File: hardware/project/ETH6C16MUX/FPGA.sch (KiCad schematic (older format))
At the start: 6 parts

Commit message: Schematic design
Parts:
- U? (x6): symbol ETH6C12MUX:iCE40HX4K-TQ144 -> ETH6C16MUX:iCE40HX4K-TQ144
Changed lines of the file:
@@
 EESchema Schematic File Version 4
-LIBS:ETH6C12MUX-cache
+LIBS:ETH6C16MUX-cache
 EELAYER 30 0
 EELAYER END
 $Descr A4 11693 8268
 encoding utf-8
-Sheet 5 8
+Sheet 4 8
 Title ""
 Date ""
@@
 $EndDescr
 $Comp
-L ETH6C12MUX:iCE40HX4K-TQ144 U?
+L ETH6C16MUX:iCE40HX4K-TQ144 U?
 U 1 1 5D7691C2
 P 2500 2550
@@
 $EndComp
 $Comp
-L ETH6C12MUX:iCE40HX4K-TQ144 U?
+L ETH6C16MUX:iCE40HX4K-TQ144 U?
 U 2 1 5D76B1F4
 P 4850 2600
@@
 $EndComp
 $Comp
-L ETH6C12MUX:iCE40HX4K-TQ144 U?
+L ETH6C16MUX:iCE40HX4K-TQ144 U?
 U 3 1 5D76D216
 P 7150 2600
@@
 $EndComp
 $Comp
-L ETH6C12MUX:iCE40HX4K-TQ144 U?
+L ETH6C16MUX:iCE40HX4K-TQ144 U?
 U 4 1 5D770CE5
 P 9350 2600
@@
 $EndComp
 $Comp
-L ETH6C12MUX:iCE40HX4K-TQ144 U?
+L ETH6C16MUX:iCE40HX4K-TQ144 U?
 U 5 1 5D7741C3
 P 5550 4750
@@
 $EndComp
 $Comp
-L ETH6C12MUX:iCE40HX4K-TQ144 U?
+L ETH6C16MUX:iCE40HX4K-TQ144 U?
 U 6 1 5D77956C
 P 2500 5100

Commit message: FPGA schematic
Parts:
- removed U? (x6): iCE40HX4K-TQ144, symbol ETH6C16MUX:iCE40HX4K-TQ144
- added C? (x2): 100n, symbol Device:C
- added C?: 47n, symbol Device:C
- added C? (x4): 1u, symbol Device:C
- added R?: 0, symbol Device:R
- added U? (x6): iCE40-HX4K-TQ144, symbol ETH6C16MUX:iCE40-HX4K-TQ144
- added U?: ASDM1-20.000MHZ-LC-T, Oscillator:Oscillator_SMD_Abracon_ASDMB-4Pin_2.5x2.0mm, symbol Oscillator:ASDMB-xxxMHz
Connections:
- net labels added: +1.2V_FPGA_VCC, +1.2V_PLL_VCC, +2.5V_FPGA_VCC, +3.3V_FPGA, CTRI_10A, CTRI_10B, CTRI_10C, CTRI_11A, CTRI_11B, CTRI_11C, CTRI_12A, CTRI_12B, CTRI_12C, CTRI_13A, CTRI_13B, CTRI_13C, CTRI_14A, CTRI_14B, CTRI_14C, CTRI_15A, CTRI_15B, CTRI_15C, CTRI_16A, CTRI_16B, CTRI_16C, CTRI_1A, CTRI_1B, CTRI_1C, CTRI_2A, CTRI_2B, CTRI_2C, CTRI_3A, CTRI_3B, CTRI_3C, CTRI_4A, CTRI_4B, CTRI_4C, CTRI_5A, CTRI_5B, CTRI_5C, CTRI_6A, CTRI_6B, CTRI_6C, CTRI_7A, CTRI_7B, CTRI_7C, CTRI_8A, CTRI_8B, CTRI_8C, CTRI_9A, CTRI_9B, CTRI_9C, CTRI_A, CTRI_B, CTRI_C, CTRI_D, CTRI_E, CTRI_F, FPGA_20MHZ_REF, FPGA_CBSEL0, FPGA_CBSEL1, FPGA_CDONE, FPGA_CFG_CS, FPGA_CRESET_B, FPGA_SPI3_CS, GND, MCU_SPI3_MISO, MCU_SPI3_MOSI, MCU_SPI3_SCLK, RELAY_CTR
- wire segments 0 -> 113
- no-connect marks 0 -> 1

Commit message: Schematic design
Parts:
- removed C?: 47n, symbol Device:C
- added C401, C403: 10u, symbol Device:C
- added C402, C404: 100n, ETH6C16MXU:C_0603_A_Pad1.05x0.95mm_HandSolder, symbol Device:C
- added D401: CDBU0520, symbol Device:D_Schottky
- added R401, R404: 100, symbol Device:R
- added R402: 220, symbol Device:R
- C405, C410: renamed from C?; footprint (none) -> ETH6C16MXU:C_0603_A_Pad1.05x0.95mm_HandSolder
- U401: renamed from U?; footprint (none) -> Package_QFP:TQFP-144_20x20mm_P0.5mm
- U402: renamed from U?; value ASDM1-20.000MHZ-LC-T -> ASDM1-100.000MHZ-LC-T
- gave numbers to parts that had none: 5
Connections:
- net labels added: +3.3V, FPGA1_CBSEL0, FPGA1_CBSEL1, FPGA1_CDONE, FPGA1_CFG_CS, FPGA1_CRESET_B, FPGA1_SPI5_CS, FPGA1_SPI5_MISO, FPGA1_SPI5_MOSI, FPGA1_SPI5_SLCK, FPGA_100MHZ_REF, RELAY0, RELAY1, RELAY10, RELAY11, RELAY12, RELAY13, RELAY14, RELAY15, RELAY16, RELAY17, RELAY18, RELAY19, RELAY2, RELAY20, RELAY21, RELAY22, RELAY23, RELAY24, RELAY25, RELAY26, RELAY27, RELAY28, RELAY29, RELAY3, RELAY30, RELAY31, RELAY32, RELAY33, RELAY34, RELAY35, RELAY36, RELAY37, RELAY38, RELAY39, RELAY4, RELAY40, RELAY41, RELAY42, RELAY43, RELAY44, RELAY45, RELAY46, RELAY47, RELAY48, RELAY49, RELAY5, RELAY50, RELAY51, RELAY52, RELAY53, RELAY6, RELAY7, RELAY8, RELAY9, RELAY[0..53]
- net labels removed: +1.2V_PLL_VCC, +2.5V_FPGA_VCC, +3.3V_FPGA, CTRI_10A, CTRI_10B, CTRI_10C, CTRI_11A, CTRI_11B, CTRI_11C, CTRI_12A, CTRI_12B, CTRI_12C, CTRI_13A, CTRI_13B, CTRI_13C, CTRI_14A, CTRI_14B, CTRI_14C, CTRI_15A, CTRI_15B, CTRI_15C, CTRI_16A, CTRI_16B, CTRI_16C, CTRI_1A, CTRI_1B, CTRI_1C, CTRI_2A, CTRI_2B, CTRI_2C, CTRI_3A, CTRI_3B, CTRI_3C, CTRI_4A, CTRI_4B, CTRI_4C, CTRI_5A, CTRI_5B, CTRI_5C, CTRI_6A, CTRI_6B, CTRI_6C, CTRI_7A, CTRI_7B, CTRI_7C, CTRI_8A, CTRI_8B, CTRI_8C, CTRI_9A, CTRI_9B, CTRI_9C, CTRI_A, CTRI_B, CTRI_C, CTRI_D, CTRI_E, CTRI_F, FPGA_20MHZ_REF, FPGA_CBSEL0, FPGA_CBSEL1, FPGA_CDONE, FPGA_CFG_CS, FPGA_CRESET_B, FPGA_SPI3_CS, RELAY_CTR
- wire segments 113 -> 134
- no-connect marks 1 -> 43
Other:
- moved on the sheet: C405, C406, C407, C408, C409, C410, R403, U401A, U401B, U401C, U401D, U401E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

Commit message: PCB design, need to redesign of the board to board connectors.
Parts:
- C401, C403: footprint (none) -> Capacitor_SMD:C_0805_2012Metric_Pad1.15x1.40mm_HandSolder
- C406, C407, C408, C409: footprint (none) -> ETH6C16MXU:C_0603_B_Pad1.05x0.95mm_HandSolder
- D401: footprint (none) -> Diode_SMD:D_SOD-523
- R401, R402, R403, R404: footprint (none) -> Resistor_SMD:R_0603_1608Metric_Pad1.05x0.95mm_HandSolder
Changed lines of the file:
@@
 F 0 "R403" V 9450 5200 50  0000 C CNN
 F 1 "0" V 9550 5200 50  0000 C CNN
-F 2 "" V 9580 5200 50  0001 C CNN
+F 2 "Resistor_SMD:R_0603_1608Metric_Pad1.05x0.95mm_HandSolder" V 9580 5200 50  0001 C CNN
 F 3 "~" H 9650 5200 50  0001 C CNN
 	1    9650 5200
@@
 F 0 "C406" H 815 7296 50  0000 L CNN
 F 1 "1u" H 815 7205 50  0000 L CNN
-F 2 "" H 738 7100 50  0001 C CNN
+F 2 "ETH6C16MXU:C_0603_B_Pad1.05x0.95mm_HandSolder" H 738 7100 50  0001 C CNN
 F 3 "~" H 700 7250 50  0001 C CNN
 	1    700  7250
@@
 F 0 "C407" H 1315 7296 50  0000 L CNN
 F 1 "1u" H 1315 7205 50  0000 L CNN
-F 2 "" H 1238 7100 50  0001 C CNN
+F 2 "ETH6C16MXU:C_0603_B_Pad1.05x0.95mm_HandSolder" H 1238 7100 50  0001 C CNN
 F 3 "~" H 1200 7250 50  0001 C CNN
 	1    1200 7250
@@
 F 0 "C408" H 1815 7296 50  0000 L CNN
 F 1 "1u" H 1815 7205 50  0000 L CNN
-F 2 "" H 1738 7100 50  0001 C CNN
+F 2 "ETH6C16MXU:C_0603_B_Pad1.05x0.95mm_HandSolder" H 1738 7100 50  0001 C CNN
 F 3 "~" H 1700 7250 50  0001 C CNN
 	1    1700 7250
@@
 F 0 "C409" H 2315 7296 50  0000 L CNN
 F 1 "1u" H 2315 7205 50  0000 L CNN
-F 2 "" H 2238 7100 50  0001 C CNN
+F 2 "ETH6C16MXU:C_0603_B_Pad1.05x0.95mm_HandSolder" H 2238 7100 50  0001 C CNN
 F 3 "~" H 2200 7250 50  0001 C CNN
 	1    2200 7250
@@
 F 0 "R402" V 2093 4950 50  0000 C CNN
 F 1 "220" V 2184 4950 50  0000 C CNN
-F 2 "" V 2230 4950 50  0001 C CNN
+F 2 "Resistor_SMD:R_0603_1608Metric_Pad1.05x0.95mm_HandSolder" V 2230 4950 50  0001 C CNN
 F 3 "~" H 2300 4950 50  0001 C CNN
 	1    2300 4950
@@
 F 0 "C401" H 5365 4746 50  0000 L CNN
 F 1 "10u" H 5365 4655 50  0000 L CNN
-F 2 "" H 5288 4550 50  0001 C CNN
+F 2 "Capacitor_SMD:C_0805_2012Metric_Pad1.15x1.40mm_HandSolder" H 5288 4550 50  0001 C CNN
 F 3 "~" H 5250 4700 50  0001 C CNN
 	1    5250 4700
@@
 F 0 "R401" V 4793 4900 50  0000 C CNN
 F 1 "100" V 4884 4900 50  0000 C CNN
-F 2 "" V 4930 4900 50  0001 C CNN
+F 2 "Resistor_SMD:R_0603_1608Metric_Pad1.05x0.95mm_HandSolder" V 4930 4900 50  0001 C CNN
 F 3 "~" H 5000 4900 50  0001 C CNN
 	1    5000 4900
@@
 F 0 "C403" H 5365 5246 50  0000 L CNN
 F 1 "10u" H 5365 5155 50  0000 L CNN
-F 2 "" H 5288 5050 50  0001 C CNN
+F 2 "Capacitor_SMD:C_0805_2012Metric_Pad1.15x1.40mm_HandSolder" H 5288 5050 50  0001 C CNN
 F 3 "~" H 5250 5200 50  0001 C CNN
 	1    5250 5200
@@
 F 0 "R404" V 4793 5400 50  0000 C CNN
 F 1 "100" V 4884 5400 50  0000 C CNN
-F 2 "" V 4930 5400 50  0001 C CNN
+F 2 "Resistor_SMD:R_0603_1608Metric_Pad1.05x0.95mm_HandSolder" V 4930 5400 50  0001 C CNN
 F 3 "~" H 5000 5400 50  0001 C CNN
 	1    5000 5400
@@
 F 0 "D401" H 6200 5684 50  0000 C CNN
 F 1 "CDBU0520" H 6200 5775 50  0000 C CNN
-F 2 "" H 6200 5900 50  0001 C CNN
+F 2 "Diode_SMD:D_SOD-523" H 6200 5900 50  0001 C CNN
 F 3 "~" H 6200 5900 50  0001 C CNN
 	1    6200 5900

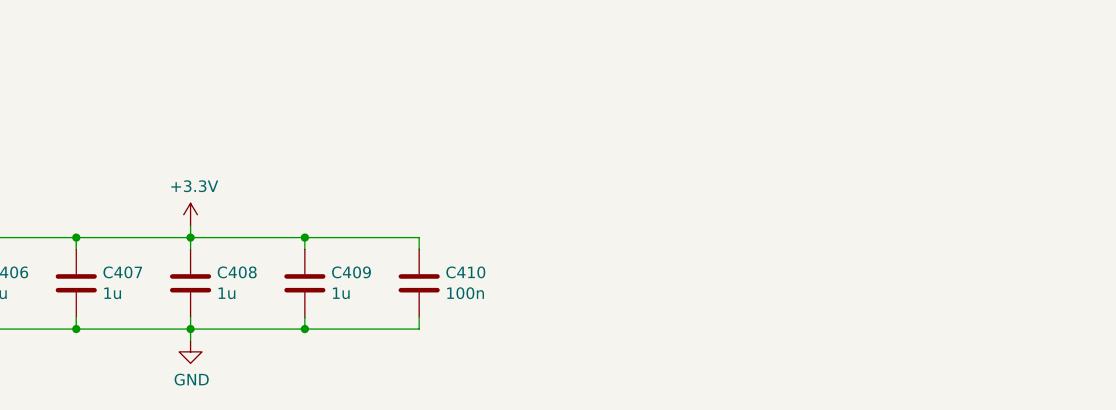
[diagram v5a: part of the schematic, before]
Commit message: PCB layout, deleted USB.
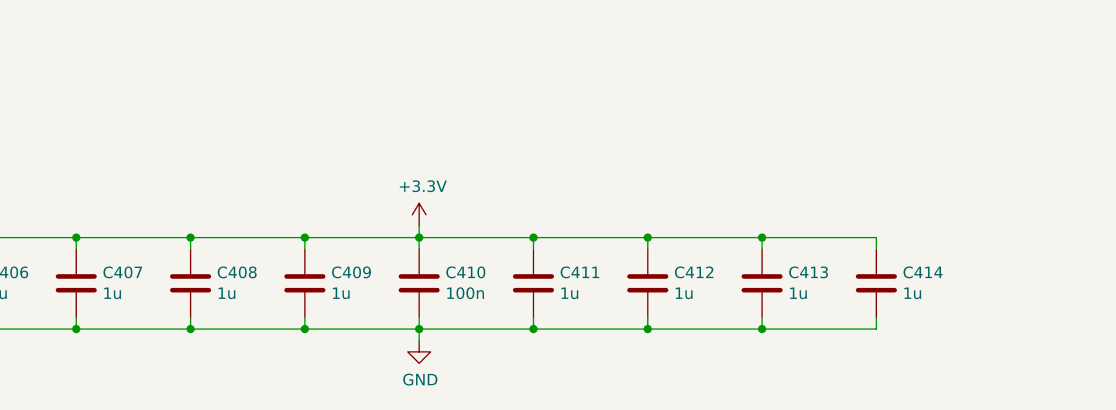
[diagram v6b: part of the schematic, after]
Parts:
- added C411, C412, C413, C414: 1u, ETH6C16MXU:C_0603_B_Pad1.05x0.95mm_HandSolder, symbol Device:C
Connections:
- net +3V3: now also C411.1, C412.1, C413.1, C414.1
- net GND: now also C411.2, C412.2, C413.2, C414.2
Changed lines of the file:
@@
 $Descr A4 11693 8268
 encoding utf-8
-Sheet 4 8
+Sheet 4 7
 Title ""
 Date ""
@@
 $EndComp
 $Comp
-L power:GND #PWR0414
-U 1 1 5DDE0555
-P 1700 7500
-F 0 "#PWR0414" H 1700 7250 50  0001 C CNN
-F 1 "GND" H 1705 7327 50  0000 C CNN
-F 2 "" H 1700 7500 50  0001 C CNN
-F 3 "" H 1700 7500 50  0001 C CNN
-	1    1700 7500
-	1    0    0    -1
-$EndComp
-$Comp
 L Device:C C407
 U 1 1 5DDE07CE
@@
 Connection ~ 1200 7050
 Wire Wire Line
-	1700 7500 1700 7450
-Wire Wire Line
-	1700 7000 1700 7050
+	2700 7000 2700 7050
 $Comp
 L Device:C C410
@@
 L power:+3.3V #PWR0413
 U 1 1 5DAA6483
-P 1700 7000
-F 0 "#PWR0413" H 1700 6850 50  0001 C CNN
-F 1 "+3.3V" H 1715 7173 50  0000 C CNN
-F 2 "" H 1700 7000 50  0001 C CNN
-F 3 "" H 1700 7000 50  0001 C CNN
-	1    1700 7000
+P 2700 7000
+F 0 "#PWR0413" H 2700 6850 50  0001 C CNN
+F 1 "+3.3V" H 2715 7173 50  0000 C CNN
+F 2 "" H 2700 7000 50  0001 C CNN
+F 3 "" H 2700 7000 50  0001 C CNN
+	1    2700 7000
 	1    0    0    -1
 $EndComp
@@
 Wire Wire Line
 	2000 2300 1950 2300
+$Comp
+L Device:C C411
+U 1 1 5D90990C
+P 3200 7250
+F 0 "C411" H 3315 7296 50  0000 L CNN
+F 1 "1u" H 3315 7205 50  0000 L CNN
+F 2 "ETH6C16MXU:C_0603_B_Pad1.05x0.95mm_HandSolder" H 3238 7100 50  0001 C CNN
+F 3 "~" H 3200 7250 50  0001 C CNN
+	1    3200 7250
+	1    0    0    -1
+$EndComp
+$Comp
+L Device:C C412
+U 1 1 5D909912
+P 3700 7250
+F 0 "C412" H 3815 7296 50  0000 L CNN
+F 1 "1u" H 3815 7205 50  0000 L CNN
+F 2 "ETH6C16MXU:C_0603_B_Pad1.05x0.95mm_HandSolder" H 3738 7100 50  0001 C CNN
+F 3 "~" H 3700 7250 50  0001 C CNN
+	1    3700 7250
+	1    0    0    -1
+$EndComp
+$Comp
+L Device:C C413
+U 1 1 5D909918
+P 4200 7250
+F 0 "C413" H 4315 7296 50  0000 L CNN
+F 1 "1u" H 4315 7205 50  0000 L CNN
+F 2 "ETH6C16MXU:C_0603_B_Pad1.05x0.95mm_HandSolder" H 4238 7100 50  0001 C CNN
+F 3 "~" H 4200 7250 50  0001 C CNN
+	1    4200 7250
+	1    0    0    -1
+$EndComp
+$Comp
+L Device:C C414
+U 1 1 5D90991E
+P 4700 7250
+F 0 "C414" H 4815 7296 50  0000 L CNN
+F 1 "1u" H 4815 7205 50  0000 L CNN
+F 2 "ETH6C16MXU:C_0603_B_Pad1.05x0.95mm_HandSolder" H 4738 7100 50  0001 C CNN
+F 3 "~" H 4700 7250 50  0001 C CNN
+	1    4700 7250
+	1    0    0    -1
+$EndComp
+Wire Wire Line
+	4700 7450 4700 7400
+Connection ~ 2700 7450
+Wire Wire Line
+	4700 7100 4700 7050
+Wire Wire Line
+	4700 7050 4200 7050
+Connection ~ 2700 7050
+Wire Wire Line
+	3200 7100 3200 7050
+Connection ~ 3200 7050
+Wire Wire Line
+	3200 7050 2700 7050
+Wire Wire Line
+	3200 7400 3200 7450
+Connection ~ 3200 7450
+Wire Wire Line
+	3200 7450 3700 7450
+Wire Wire Line
+	3700 7400 3700 7450
+Connection ~ 3700 7450
+Wire Wire Line
+	3700 7450 4200 7450
+Wire Wire Line
+	3700 7100 3700 7050
+Connection ~ 3700 7050
+Wire Wire Line
+	3700 7050 3200 7050
+Wire Wire Line
+	4200 7100 4200 7050
+Connection ~ 4200 7050
+Wire Wire Line
+	4200 7050 3700 7050
+Wire Wire Line
+	4200 7400 4200 7450
+Connection ~ 4200 7450
+Wire Wire Line
+	4200 7450 4700 7450
+Wire Wire Line
+	2700 7450 3200 7450
+Wire Wire Line
+	2700 7500 2700 7450
+$Comp
+L power:GND #PWR0414
+U 1 1 5DDE0555
+P 2700 7500
+F 0 "#PWR0414" H 2700 7250 50  0001 C CNN
+F 1 "GND" H 2705 7327 50  0000 C CNN
+F 2 "" H 2700 7500 50  0001 C CNN
+F 3 "" H 2700 7500 50  0001 C CNN
+	1    2700 7500
+	1    0    0    -1
+$EndComp
 Wire Bus Line
 	3650 750  3650 3650

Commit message: Deleted FPGA part and change it for SPI IO chips. Change power supply circuit.
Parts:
- C402, C404, C405, C410: footprint ETH6C16MXU:C_0603_A_Pad1.05x0.95mm_HandSolder -> Capacitor_SMD:C_0603_1608Metric_Pad1.05x0.95mm_HandSolder
- C406, C407, C408, C409, C411, C412, C413, C414: footprint ETH6C16MXU:C_0603_B_Pad1.05x0.95mm_HandSolder -> Capacitor_SMD:C_0603_1608Metric_Pad1.05x0.95mm_HandSolder
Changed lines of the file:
@@
 F 0 "C405" H 1035 5346 50  0000 R CNN
 F 1 "100n" H 1035 5255 50  0000 R CNN
-F 2 "ETH6C16MXU:C_0603_A_Pad1.05x0.95mm_HandSolder" H 1188 5150 50  0001 C CNN
+F 2 "Capacitor_SMD:C_0603_1608Metric_Pad1.05x0.95mm_HandSolder" H 1188 5150 50  0001 C CNN
 F 3 "~" H 1150 5300 50  0001 C CNN
 	1    1150 5300
@@
 F 0 "C406" H 815 7296 50  0000 L CNN
 F 1 "1u" H 815 7205 50  0000 L CNN
-F 2 "ETH6C16MXU:C_0603_B_Pad1.05x0.95mm_HandSolder" H 738 7100 50  0001 C CNN
+F 2 "Capacitor_SMD:C_0603_1608Metric_Pad1.05x0.95mm_HandSolder" H 738 7100 50  0001 C CNN
 F 3 "~" H 700 7250 50  0001 C CNN
 	1    700  7250
@@
 F 0 "C407" H 1315 7296 50  0000 L CNN
 F 1 "1u" H 1315 7205 50  0000 L CNN
-F 2 "ETH6C16MXU:C_0603_B_Pad1.05x0.95mm_HandSolder" H 1238 7100 50  0001 C CNN
+F 2 "Capacitor_SMD:C_0603_1608Metric_Pad1.05x0.95mm_HandSolder" H 1238 7100 50  0001 C CNN
 F 3 "~" H 1200 7250 50  0001 C CNN
 	1    1200 7250
@@
 F 0 "C408" H 1815 7296 50  0000 L CNN
 F 1 "1u" H 1815 7205 50  0000 L CNN
-F 2 "ETH6C16MXU:C_0603_B_Pad1.05x0.95mm_HandSolder" H 1738 7100 50  0001 C CNN
+F 2 "Capacitor_SMD:C_0603_1608Metric_Pad1.05x0.95mm_HandSolder" H 1738 7100 50  0001 C CNN
 F 3 "~" H 1700 7250 50  0001 C CNN
 	1    1700 7250
@@
 F 0 "C409" H 2315 7296 50  0000 L CNN
 F 1 "1u" H 2315 7205 50  0000 L CNN
-F 2 "ETH6C16MXU:C_0603_B_Pad1.05x0.95mm_HandSolder" H 2238 7100 50  0001 C CNN
+F 2 "Capacitor_SMD:C_0603_1608Metric_Pad1.05x0.95mm_HandSolder" H 2238 7100 50  0001 C CNN
 F 3 "~" H 2200 7250 50  0001 C CNN
 	1    2200 7250
@@
 F 0 "C410" H 2815 7296 50  0000 L CNN
 F 1 "100n" H 2815 7205 50  0000 L CNN
-F 2 "ETH6C16MXU:C_0603_A_Pad1.05x0.95mm_HandSolder" H 2738 7100 50  0001 C CNN
+F 2 "Capacitor_SMD:C_0603_1608Metric_Pad1.05x0.95mm_HandSolder" H 2738 7100 50  0001 C CNN
 F 3 "~" H 2700 7250 50  0001 C CNN
 	1    2700 7250
@@
 F 0 "C402" H 5865 4746 50  0000 L CNN
 F 1 "100n" H 5865 4655 50  0000 L CNN
-F 2 "ETH6C16MXU:C_0603_A_Pad1.05x0.95mm_HandSolder" H 5788 4550 50  0001 C CNN
+F 2 "Capacitor_SMD:C_0603_1608Metric_Pad1.05x0.95mm_HandSolder" H 5788 4550 50  0001 C CNN
 F 3 "~" H 5750 4700 50  0001 C CNN
 	1    5750 4700
@@
 F 0 "C404" H 5865 5246 50  0000 L CNN
 F 1 "100n" H 5865 5155 50  0000 L CNN
-F 2 "ETH6C16MXU:C_0603_A_Pad1.05x0.95mm_HandSolder" H 5788 5050 50  0001 C CNN
+F 2 "Capacitor_SMD:C_0603_1608Metric_Pad1.05x0.95mm_HandSolder" H 5788 5050 50  0001 C CNN
 F 3 "~" H 5750 5200 50  0001 C CNN
 	1    5750 5200
@@
 F 0 "C411" H 3315 7296 50  0000 L CNN
 F 1 "1u" H 3315 7205 50  0000 L CNN
-F 2 "ETH6C16MXU:C_0603_B_Pad1.05x0.95mm_HandSolder" H 3238 7100 50  0001 C CNN
+F 2 "Capacitor_SMD:C_0603_1608Metric_Pad1.05x0.95mm_HandSolder" H 3238 7100 50  0001 C CNN
 F 3 "~" H 3200 7250 50  0001 C CNN
 	1    3200 7250
@@
 F 0 "C412" H 3815 7296 50  0000 L CNN
 F 1 "1u" H 3815 7205 50  0000 L CNN
-F 2 "ETH6C16MXU:C_0603_B_Pad1.05x0.95mm_HandSolder" H 3738 7100 50  0001 C CNN
+F 2 "Capacitor_SMD:C_0603_1608Metric_Pad1.05x0.95mm_HandSolder" H 3738 7100 50  0001 C CNN
 F 3 "~" H 3700 7250 50  0001 C CNN
 	1    3700 7250
@@
 F 0 "C413" H 4315 7296 50  0000 L CNN
 F 1 "1u" H 4315 7205 50  0000 L CNN
-F 2 "ETH6C16MXU:C_0603_B_Pad1.05x0.95mm_HandSolder" H 4238 7100 50  0001 C CNN
+F 2 "Capacitor_SMD:C_0603_1608Metric_Pad1.05x0.95mm_HandSolder" H 4238 7100 50  0001 C CNN
 F 3 "~" H 4200 7250 50  0001 C CNN
 	1    4200 7250
@@
 F 0 "C414" H 4815 7296 50  0000 L CNN
 F 1 "1u" H 4815 7205 50  0000 L CNN
-F 2 "ETH6C16MXU:C_0603_B_Pad1.05x0.95mm_HandSolder" H 4738 7100 50  0001 C CNN
+F 2 "Capacitor_SMD:C_0603_1608Metric_Pad1.05x0.95mm_HandSolder" H 4738 7100 50  0001 C CNN
 F 3 "~" H 4700 7250 50  0001 C CNN
 	1    4700 7250
